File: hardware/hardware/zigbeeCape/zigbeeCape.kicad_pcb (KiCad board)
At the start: 4 copper layers, 63.5 x 54.6 mm, 160 parts, among them J1 Conn_ARM_JTAG_SWD_10, SW1 SW_MEC_5E, SW2 SW_MEC_5E, SW3 SW_MEC_5E, SW4 SW_MEC_5E, SW5 SW_MEC_5E, U1 CC1352R, U2 0.8Ghz_and_2.4GHz_Filter, U3 SMA_Antenna, U4 BeagleBone_P8, U5 BeagleBone_P9, Y1 32.768kHz, Y2 48MHz

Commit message: Almost done with traces
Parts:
- removed the REF** at (25.4, -8.89)
- removed the REF** at (33.1, -25.1)
- removed the REF** at (33.1, -27.7)
- removed the REF** at (33.1, -30.2)
- removed the REF** at (42.8, -14.1)
- removed the REF** at (42.2, -11.2)
- removed the REF** at (49.0, -14.6)
- removed the REF** at (27.1, -10.3)
- removed the REF** at (37.5, -7.49)
- removed the REF** at (28.6, -11.6)
- removed the REF** at (30.1, -13.1)
- removed the REF** at (31.8, -14.6)
- removed the REF** at (33.0, -15.9)
- removed the REF** at (33.1, -17.5)
- removed the REF** at (33.1, -20.1)
- removed the REF** at (33.1, -22.6)
- C10, C11, C13, C15, C16, C6, C8, C9, L1: moved to B.Cu
- moved C14 46.1 mm to (30.1, -21.6)
- moved C31 41.3 mm to (19.4, -30.0)
- moved Y1 39.9 mm to (31.5, -24.8), turned to 180 degrees
- moved C12 39.7 mm to (32.6, -21.6)
- moved R9 11.1 mm to (49.0, -37.6), turned to 90 degrees
- moved C13 9.39 mm to (38.5, -40.3), turned to 180 degrees
- moved R5 7.75 mm to (48.3, -30.7)
- moved C11 7.15 mm to (37.7, -43.6), turned to 180 degrees
- moved D3 6.98 mm to (48.4, -34.9)
- moved C5 6.55 mm to (43.1, -39.6), turned to 0 degrees
- moved C16 6.38 mm to (37.7, -41.9), turned to 180 degrees
- moved C8 4.66 mm to (41.9, -29.5), turned to 180 degrees
- moved Y2 3.68 mm to (39.9, -42.4), turned to 45 degrees
- moved C15 3.66 mm to (45.5, -29.5)
- moved C6 3.46 mm to (37.7, -29.5), turned to 180 degrees
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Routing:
- net SPI_CS: track 17.5 -> 38.0 mm
- net UART_RX: track 11.5 -> 29.0 mm
- net UART_TX: track 13.4 -> 30.2 mm
- net Net-(C14-Pad1): track 0.00 -> 16.4 mm
- net Net-(C12-Pad1): track 0.00 -> 15.2 mm
- net SPI_MISO: track 20.3 -> 33.2 mm
- net /ZigBeeFiltering/RX_TX: track 17.8 -> 8.64 mm, vias 3 -> 2
- net Cape_HeartBeat: track 10.8 -> 2.47 mm, vias 2 -> 0
- net Aux_1: track 14.9 -> 22.3 mm
- net VDDR: track 5.64 -> 11.8 mm, vias 0 -> 2
- net Aux_2: track 14.4 -> 20.1 mm
- net Net-(U1-Pad47): track 0.29 -> 5.15 mm
- net Net-(U1-Pad46): track 0.00 -> 4.84 mm
- net Net-(J1-Pad2): track 13.3 -> 17.8 mm
- net Net-(C15-Pad1): track 0.00 -> 4.32 mm, vias 0 -> 1
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
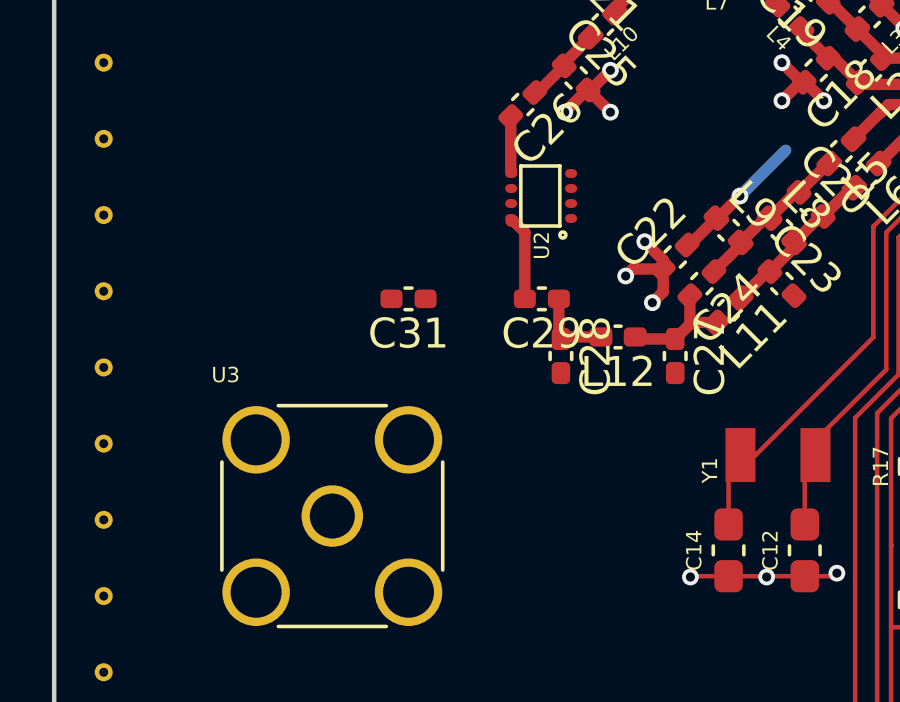
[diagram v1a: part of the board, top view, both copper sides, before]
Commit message: Finished traces, a couple problems with the design rules
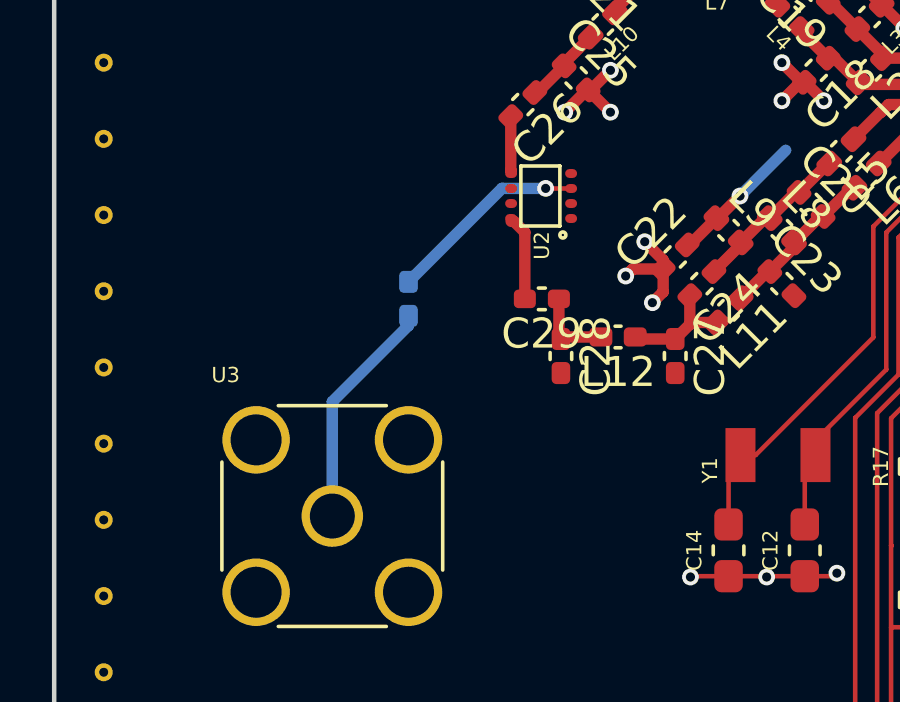
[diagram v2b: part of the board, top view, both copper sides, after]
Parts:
- C31: moved to B.Cu
- turned C31 to 270 degrees
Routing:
- net Net-(C31-Pad2): track 0.00 -> 7.79 mm
- net Net-(C31-Pad1): track 0.00 -> 6.71 mm, vias 0 -> 1

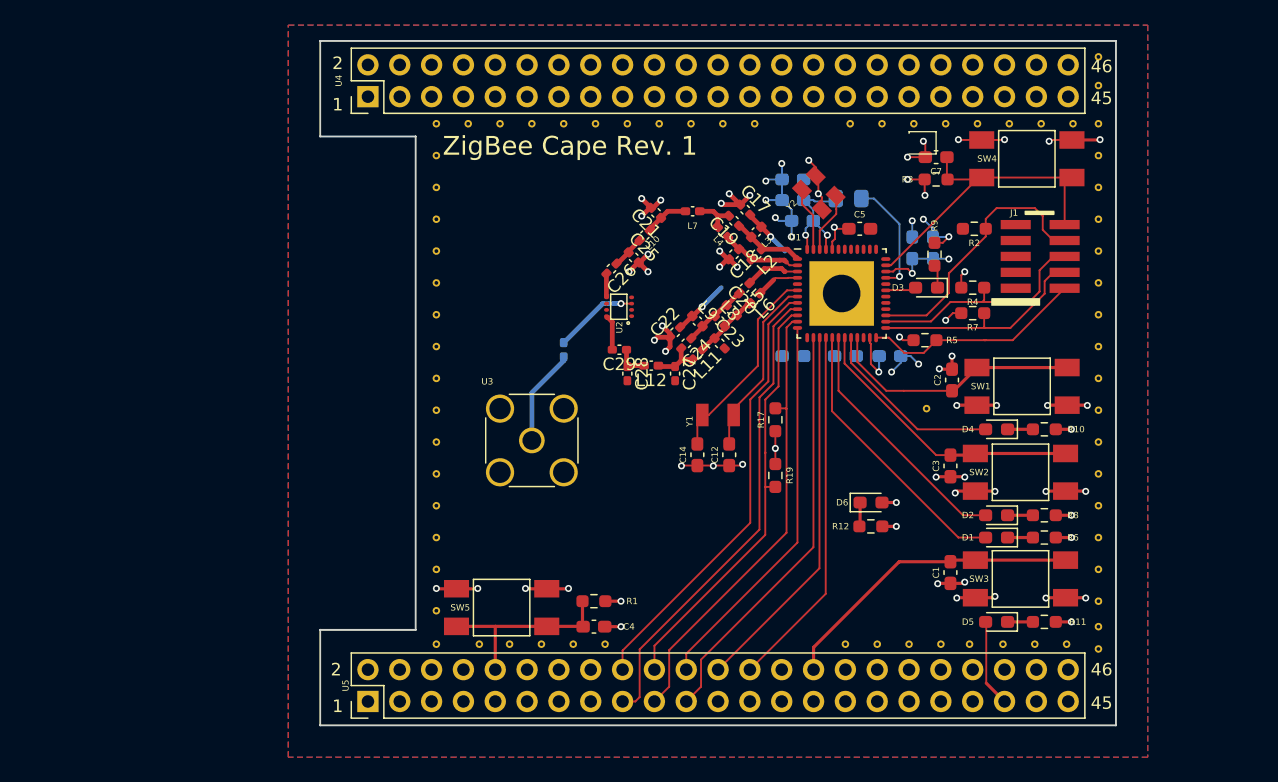
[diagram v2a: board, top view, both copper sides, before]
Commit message: Fixed some trace spacing things
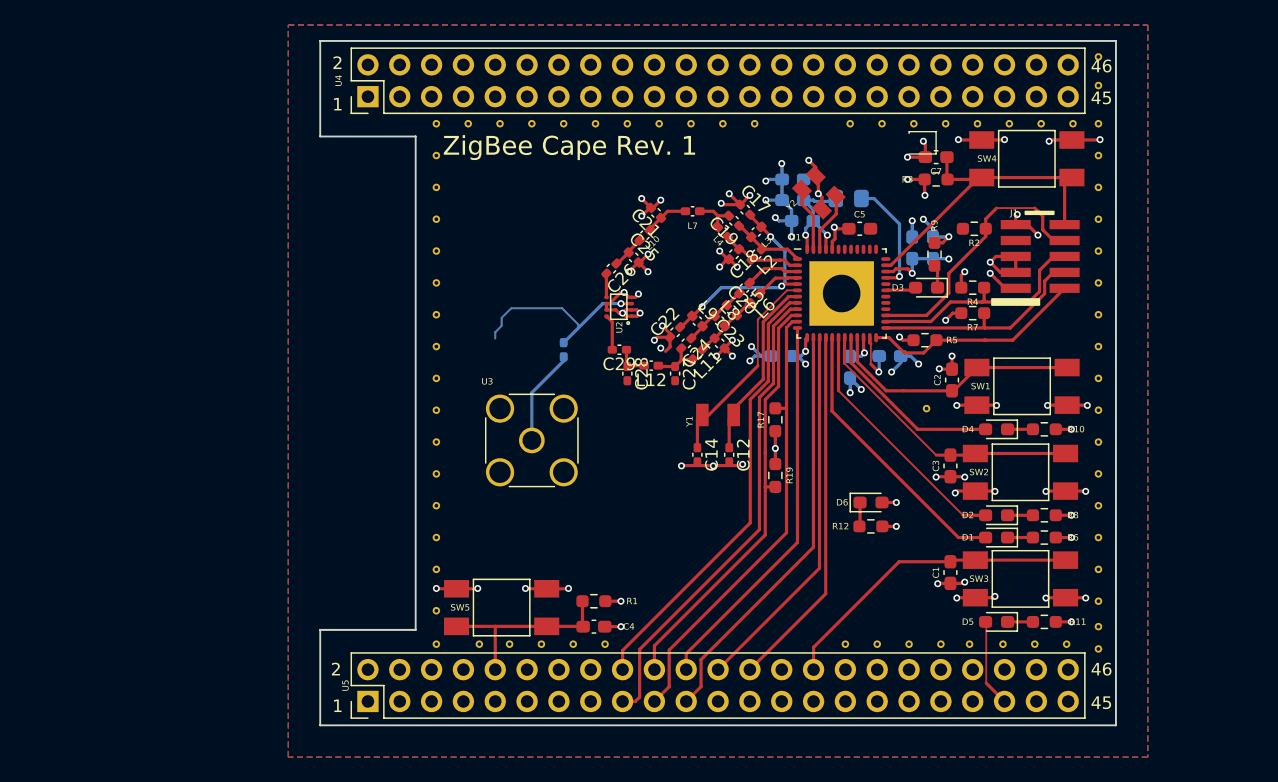
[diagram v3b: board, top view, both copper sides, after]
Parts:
- C12, C14: footprint Capacitor_SMD:C_0603_1608Metric_Pad1.08x0.95mm_HandSolder -> Capacitor_SMD:C_0402_1005Metric_Pad0.74x0.62mm_HandSolder
- R3: value DNM_10K -> DNM_10k
- moved C8 0.97 mm to (42.3, -28.6), turned to 270 degrees
- moved C6 0.89 mm to (36.8, -29.5)
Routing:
- net GND: track 99.9 -> 125.9 mm, vias 67 -> 81
- net Net-(C31-Pad1): track 6.71 -> 15.8 mm
- net /ZigBeeFiltering/RX_TX: track 8.64 -> 17.7 mm, vias 2 -> 3
- net +3V3: track 17.2 -> 25.9 mm, vias 8 -> 12
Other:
- net class Default: clearance 0.254 -> 0.1524
- net class HighSpeed added: clearance 0.127, trace_width 0.381, via_dia 0.5588, via_drill 0.3048
- rule trace_clearance: 0.254 -> 0.1524

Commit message: Finished up the stitching vias
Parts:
- added REF**: ViaStitch-0.6mm, zigbeeCape:ViaStitch-0.6mm, F.Cu at (46.9, -23.5)
- added REF**: ViaStitch-0.6mm, zigbeeCape:ViaStitch-0.6mm, F.Cu at (45.0, -43.2)
- added REF**: ViaStitch-0.6mm, zigbeeCape:ViaStitch-0.6mm, F.Cu at (9.27, -27.7)
- added REF**: ViaStitch-0.6mm, zigbeeCape:ViaStitch-0.6mm, F.Cu at (22.0, -30.2)
- added REF**: ViaStitch-0.6mm, zigbeeCape:ViaStitch-0.6mm, F.Cu at (16.9, -30.2)
- added REF**: ViaStitch-0.6mm, zigbeeCape:ViaStitch-0.6mm, F.Cu at (14.4, -30.2)
- added REF**: ViaStitch-0.6mm, zigbeeCape:ViaStitch-0.6mm, F.Cu at (11.8, -30.2)
- added REF**: ViaStitch-0.6mm, zigbeeCape:ViaStitch-0.6mm, F.Cu at (9.27, -30.2)
- added REF**: ViaStitch-0.6mm, zigbeeCape:ViaStitch-0.6mm, F.Cu at (19.4, -32.8)
- added REF**: ViaStitch-0.6mm, zigbeeCape:ViaStitch-0.6mm, F.Cu at (16.9, -32.8)
- added REF**: ViaStitch-0.6mm, zigbeeCape:ViaStitch-0.6mm, F.Cu at (14.4, -32.8)
- added REF**: ViaStitch-0.6mm, zigbeeCape:ViaStitch-0.6mm, F.Cu at (11.8, -32.8)
- added REF**: ViaStitch-0.6mm, zigbeeCape:ViaStitch-0.6mm, F.Cu at (42.3, -43.8)
- added REF**: ViaStitch-0.6mm, zigbeeCape:ViaStitch-0.6mm, F.Cu at (9.27, -32.8)
- added REF**: ViaStitch-0.6mm, zigbeeCape:ViaStitch-0.6mm, F.Cu at (21.6, -35.3)
- added REF**: ViaStitch-0.6mm, zigbeeCape:ViaStitch-0.6mm, F.Cu at (19.4, -35.3)
- added REF**: ViaStitch-0.6mm, zigbeeCape:ViaStitch-0.6mm, F.Cu at (16.9, -35.3)
- added REF**: ViaStitch-0.6mm, zigbeeCape:ViaStitch-0.6mm, F.Cu at (14.4, -35.3)
- added REF**: ViaStitch-0.6mm, zigbeeCape:ViaStitch-0.6mm, F.Cu at (11.8, -35.3)
- added REF**: ViaStitch-0.6mm, zigbeeCape:ViaStitch-0.6mm, F.Cu at (9.27, -35.3)
- added REF**: ViaStitch-0.6mm, zigbeeCape:ViaStitch-0.6mm, F.Cu at (22.0, -37.8)
- added REF**: ViaStitch-0.6mm, zigbeeCape:ViaStitch-0.6mm, F.Cu at (19.4, -37.8)
- added REF**: ViaStitch-0.6mm, zigbeeCape:ViaStitch-0.6mm, F.Cu at (16.9, -37.8)
- added REF**: ViaStitch-0.6mm, zigbeeCape:ViaStitch-0.6mm, F.Cu at (44.8, -45.5)
- added REF**: ViaStitch-0.6mm, zigbeeCape:ViaStitch-0.6mm, F.Cu at (14.4, -37.8)
- added REF**: ViaStitch-0.6mm, zigbeeCape:ViaStitch-0.6mm, F.Cu at (11.8, -37.8)
- added REF**: ViaStitch-0.6mm, zigbeeCape:ViaStitch-0.6mm, F.Cu at (9.27, -37.8)
- added REF**: ViaStitch-0.6mm, zigbeeCape:ViaStitch-0.6mm, F.Cu at (24.5, -40.4)
- added REF**: ViaStitch-0.6mm, zigbeeCape:ViaStitch-0.6mm, F.Cu at (22.0, -40.4)
- added REF**: ViaStitch-0.6mm, zigbeeCape:ViaStitch-0.6mm, F.Cu at (19.4, -40.4)
- added REF**: ViaStitch-0.6mm, zigbeeCape:ViaStitch-0.6mm, F.Cu at (16.9, -40.4)
- added REF**: ViaStitch-0.6mm, zigbeeCape:ViaStitch-0.6mm, F.Cu at (14.4, -40.4)
- added REF**: ViaStitch-0.6mm, zigbeeCape:ViaStitch-0.6mm, F.Cu at (11.8, -40.4)
- added REF**: ViaStitch-0.6mm, zigbeeCape:ViaStitch-0.6mm, F.Cu at (9.27, -40.4)
- added REF**: ViaStitch-0.6mm, zigbeeCape:ViaStitch-0.6mm, F.Cu at (42.3, -45.5)
- added REF**: ViaStitch-0.6mm, zigbeeCape:ViaStitch-0.6mm, F.Cu at (27.1, -42.9)
- added REF**: ViaStitch-0.6mm, zigbeeCape:ViaStitch-0.6mm, F.Cu at (24.5, -42.9)
- added REF**: ViaStitch-0.6mm, zigbeeCape:ViaStitch-0.6mm, F.Cu at (22.0, -42.9)
- added REF**: ViaStitch-0.6mm, zigbeeCape:ViaStitch-0.6mm, F.Cu at (19.4, -42.9)
- added REF**: ViaStitch-0.6mm, zigbeeCape:ViaStitch-0.6mm, F.Cu at (16.9, -42.9)
- added REF**: ViaStitch-0.6mm, zigbeeCape:ViaStitch-0.6mm, F.Cu at (14.4, -42.9)
- added REF**: ViaStitch-0.6mm, zigbeeCape:ViaStitch-0.6mm, F.Cu at (11.8, -42.9)
- added REF**: ViaStitch-0.6mm, zigbeeCape:ViaStitch-0.6mm, F.Cu at (9.27, -42.9)
- added REF**: ViaStitch-0.6mm, zigbeeCape:ViaStitch-0.6mm, F.Cu at (27.1, -45.5)
- added REF**: ViaStitch-0.6mm, zigbeeCape:ViaStitch-0.6mm, F.Cu at (24.5, -45.5)
- added REF**: ViaStitch-0.6mm, zigbeeCape:ViaStitch-0.6mm, F.Cu at (44.8, -48.0)
- added REF**: ViaStitch-0.6mm, zigbeeCape:ViaStitch-0.6mm, F.Cu at (22.0, -45.5)
- added REF**: ViaStitch-0.6mm, zigbeeCape:ViaStitch-0.6mm, F.Cu at (19.4, -45.5)
- added REF**: ViaStitch-0.6mm, zigbeeCape:ViaStitch-0.6mm, F.Cu at (16.9, -45.5)
- added REF**: ViaStitch-0.6mm, zigbeeCape:ViaStitch-0.6mm, F.Cu at (14.4, -45.5)
- added REF**: ViaStitch-0.6mm, zigbeeCape:ViaStitch-0.6mm, F.Cu at (11.8, -45.5)
- added REF**: ViaStitch-0.6mm, zigbeeCape:ViaStitch-0.6mm, F.Cu at (9.27, -45.5)
- added REF**: ViaStitch-0.6mm, zigbeeCape:ViaStitch-0.6mm, F.Cu at (27.1, -48.0)
- added REF**: ViaStitch-0.6mm, zigbeeCape:ViaStitch-0.6mm, F.Cu at (24.5, -48.0)
- added REF**: ViaStitch-0.6mm, zigbeeCape:ViaStitch-0.6mm, F.Cu at (22.0, -48.0)
- added REF**: ViaStitch-0.6mm, zigbeeCape:ViaStitch-0.6mm, F.Cu at (19.4, -48.0)
- added REF**: ViaStitch-0.6mm, zigbeeCape:ViaStitch-0.6mm, F.Cu at (34.3, -43.6)
- added REF**: ViaStitch-0.6mm, zigbeeCape:ViaStitch-0.6mm, F.Cu at (16.9, -48.0)
- added REF**: ViaStitch-0.6mm, zigbeeCape:ViaStitch-0.6mm, F.Cu at (14.4, -48.0)
- added REF**: ViaStitch-0.6mm, zigbeeCape:ViaStitch-0.6mm, F.Cu at (11.8, -48.0)
- added REF**: ViaStitch-0.6mm, zigbeeCape:ViaStitch-0.6mm, F.Cu at (52.3, -42.8)
- added REF**: ViaStitch-0.6mm, zigbeeCape:ViaStitch-0.6mm, F.Cu at (56.4, -43.7)
- added REF**: ViaStitch-0.6mm, zigbeeCape:ViaStitch-0.6mm, F.Cu at (58.3, -42.4)
- added REF**: ViaStitch-0.6mm, zigbeeCape:ViaStitch-0.6mm, F.Cu at (51.6, -46.4)
- added REF**: ViaStitch-0.6mm, zigbeeCape:ViaStitch-0.6mm, F.Cu at (54.7, -46.0)
- added REF**: ViaStitch-0.6mm, zigbeeCape:ViaStitch-0.6mm, F.Cu at (57.9, -45.8)
- added REF**: ViaStitch-0.6mm, zigbeeCape:ViaStitch-0.6mm, F.Cu at (60.1, -31.4)
- added REF**: ViaStitch-0.6mm, zigbeeCape:ViaStitch-0.6mm, F.Cu at (31.8, -43.6)
- added REF**: ViaStitch-0.6mm, zigbeeCape:ViaStitch-0.6mm, F.Cu at (59.8, -34.4)
- added REF**: ViaStitch-0.6mm, zigbeeCape:ViaStitch-0.6mm, F.Cu at (57.7, -32.6)
- added REF**: ViaStitch-0.6mm, zigbeeCape:ViaStitch-0.6mm, F.Cu at (57.7, -30.7)
- added REF**: ViaStitch-0.6mm, zigbeeCape:ViaStitch-0.6mm, F.Cu at (54.5, -30.6)
- added REF**: ViaStitch-0.6mm, zigbeeCape:ViaStitch-0.6mm, F.Cu at (57.4, -28.3)
- added REF**: ViaStitch-0.6mm, zigbeeCape:ViaStitch-0.6mm, F.Cu at (54.4, -28.4)
- added REF**: ViaStitch-0.6mm, zigbeeCape:ViaStitch-0.6mm, F.Cu at (57.4, -21.5)
- added REF**: ViaStitch-0.6mm, zigbeeCape:ViaStitch-0.6mm, F.Cu at (54.2, -21.5)
- added REF**: ViaStitch-0.6mm, zigbeeCape:ViaStitch-0.6mm, F.Cu at (44.6, -9.91)
- added REF**: ViaStitch-0.6mm, zigbeeCape:ViaStitch-0.6mm, F.Cu at (47.2, -12.2)
- added REF**: ViaStitch-0.6mm, zigbeeCape:ViaStitch-0.6mm, F.Cu at (29.6, -42.9)
- added REF**: ViaStitch-0.6mm, zigbeeCape:ViaStitch-0.6mm, F.Cu at (50.3, -9.40)
- added REF**: ViaStitch-0.6mm, zigbeeCape:ViaStitch-0.6mm, F.Cu at (46.5, -15.5)
- added REF**: ViaStitch-0.6mm, zigbeeCape:ViaStitch-0.6mm, F.Cu at (49.1, -15.7)
- added REF**: ViaStitch-0.6mm, zigbeeCape:ViaStitch-0.6mm, F.Cu at (42.7, -14.4)
- added REF**: ViaStitch-0.6mm, zigbeeCape:ViaStitch-0.6mm, F.Cu at (42.5, -21.0)
- added REF**: ViaStitch-0.6mm, zigbeeCape:ViaStitch-0.6mm, F.Cu at (41.5, -23.5)
- added REF**: ViaStitch-0.6mm, zigbeeCape:ViaStitch-0.6mm, F.Cu at (41.3, -10.7)
- added REF**: ViaStitch-0.6mm, zigbeeCape:ViaStitch-0.6mm, F.Cu at (38.1, -7.37)
- added REF**: ViaStitch-0.6mm, zigbeeCape:ViaStitch-0.6mm, F.Cu at (57.5, -12.1)
- added REF**: ViaStitch-0.6mm, zigbeeCape:ViaStitch-0.6mm, F.Cu at (54.2, -12.1)
- added REF**: ViaStitch-0.6mm, zigbeeCape:ViaStitch-0.6mm, F.Cu at (34.7, -45.5)
- added REF**: ViaStitch-0.6mm, zigbeeCape:ViaStitch-0.6mm, F.Cu at (32.1, -45.5)
- added REF**: ViaStitch-0.6mm, zigbeeCape:ViaStitch-0.6mm, F.Cu at (44.2, -26.2)
- added REF**: ViaStitch-0.6mm, zigbeeCape:ViaStitch-0.6mm, F.Cu at (29.6, -45.5)
- added REF**: ViaStitch-0.6mm, zigbeeCape:ViaStitch-0.6mm, F.Cu at (34.7, -48.0)
- added REF**: ViaStitch-0.6mm, zigbeeCape:ViaStitch-0.6mm, F.Cu at (32.1, -48.0)
- added REF**: ViaStitch-0.6mm, zigbeeCape:ViaStitch-0.6mm, F.Cu at (25.3, -36.4)
- added REF**: ViaStitch-0.6mm, zigbeeCape:ViaStitch-0.6mm, F.Cu at (28.2, -36.6)
- added REF**: ViaStitch-0.6mm, zigbeeCape:ViaStitch-0.6mm, F.Cu at (26.7, -35.3)
- added REF**: ViaStitch-0.6mm, zigbeeCape:ViaStitch-0.6mm, F.Cu at (27.6, -38.0)
- added REF**: ViaStitch-0.6mm, zigbeeCape:ViaStitch-0.6mm, F.Cu at (30.5, -37.6)
- added REF**: ViaStitch-0.6mm, zigbeeCape:ViaStitch-0.6mm, F.Cu at (29.2, -39.1)
- added REF**: ViaStitch-0.6mm, zigbeeCape:ViaStitch-0.6mm, F.Cu at (27.3, -39.6)
- added REF**: ViaStitch-0.6mm, zigbeeCape:ViaStitch-0.6mm, F.Cu at (47.1, -28.6)
- added REF**: ViaStitch-0.6mm, zigbeeCape:ViaStitch-0.6mm, F.Cu at (28.4, -40.8)
- added REF**: ViaStitch-0.6mm, zigbeeCape:ViaStitch-0.6mm, F.Cu at (30.1, -40.8)
- added REF**: ViaStitch-0.6mm, zigbeeCape:ViaStitch-0.6mm, F.Cu at (31.1, -39.5)
- added REF**: ViaStitch-0.6mm, zigbeeCape:ViaStitch-0.6mm, F.Cu at (32.8, -36.7)
- added REF**: ViaStitch-0.6mm, zigbeeCape:ViaStitch-0.6mm, F.Cu at (29.7, -35.7)
- added REF**: ViaStitch-0.6mm, zigbeeCape:ViaStitch-0.6mm, F.Cu at (27.9, -34.3)
- added REF**: ViaStitch-0.6mm, zigbeeCape:ViaStitch-0.6mm, F.Cu at (26.0, -32.9)
- added REF**: ViaStitch-0.6mm, zigbeeCape:ViaStitch-0.6mm, F.Cu at (25.8, -31.0)
- added REF**: ViaStitch-0.6mm, zigbeeCape:ViaStitch-0.6mm, F.Cu at (24.4, -32.3)
- added REF**: ViaStitch-0.6mm, zigbeeCape:ViaStitch-0.6mm, F.Cu at (30.2, -29.0)
- added REF**: ViaStitch-0.6mm, zigbeeCape:ViaStitch-0.6mm, F.Cu at (47.2, -34.5)
- added REF**: ViaStitch-0.6mm, zigbeeCape:ViaStitch-0.6mm, F.Cu at (32.6, -29.2)
- added REF**: ViaStitch-0.6mm, zigbeeCape:ViaStitch-0.6mm, F.Cu at (31.2, -27.8)
- added REF**: ViaStitch-0.6mm, zigbeeCape:ViaStitch-0.6mm, F.Cu at (28.7, -27.4)
- added REF**: ViaStitch-0.6mm, zigbeeCape:ViaStitch-0.6mm, F.Cu at (28.8, -24.9)
- added REF**: ViaStitch-0.6mm, zigbeeCape:ViaStitch-0.6mm, F.Cu at (25.7, -11.3)
- added REF**: ViaStitch-0.6mm, zigbeeCape:ViaStitch-0.6mm, F.Cu at (15.9, -10.2)
- added REF**: ViaStitch-0.6mm, zigbeeCape:ViaStitch-0.6mm, F.Cu at (13.0, -10.2)
- added REF**: ViaStitch-0.6mm, zigbeeCape:ViaStitch-0.6mm, F.Cu at (31.8, -17.4)
- added REF**: ViaStitch-0.6mm, zigbeeCape:ViaStitch-0.6mm, F.Cu at (31.8, -19.8)
- added REF**: ViaStitch-0.6mm, zigbeeCape:ViaStitch-0.6mm, F.Cu at (29.6, -21.0)
- added REF**: ViaStitch-0.6mm, zigbeeCape:ViaStitch-0.6mm, F.Cu at (40.1, -46.7)
- added REF**: ViaStitch-0.6mm, zigbeeCape:ViaStitch-0.6mm, F.Cu at (29.5, -18.5)
- added REF**: ViaStitch-0.6mm, zigbeeCape:ViaStitch-0.6mm, F.Cu at (29.5, -16.0)
- added REF**: ViaStitch-0.6mm, zigbeeCape:ViaStitch-0.6mm, F.Cu at (27.1, -12.4)
- added REF**: ViaStitch-0.6mm, zigbeeCape:ViaStitch-0.6mm, F.Cu at (24.5, -12.4)
- added REF**: ViaStitch-0.6mm, zigbeeCape:ViaStitch-0.6mm, F.Cu at (22.0, -12.4)
- added REF**: ViaStitch-0.6mm, zigbeeCape:ViaStitch-0.6mm, F.Cu at (19.4, -12.4)
- added REF**: ViaStitch-0.6mm, zigbeeCape:ViaStitch-0.6mm, F.Cu at (16.9, -12.4)
- added REF**: ViaStitch-0.6mm, zigbeeCape:ViaStitch-0.6mm, F.Cu at (14.4, -12.4)
- added REF**: ViaStitch-0.6mm, zigbeeCape:ViaStitch-0.6mm, F.Cu at (11.8, -12.4)
- added REF**: ViaStitch-0.6mm, zigbeeCape:ViaStitch-0.6mm, F.Cu at (9.27, -12.4)
- added REF**: ViaStitch-0.6mm, zigbeeCape:ViaStitch-0.6mm, F.Cu at (37.6, -47.0)
- added REF**: ViaStitch-0.6mm, zigbeeCape:ViaStitch-0.6mm, F.Cu at (27.1, -15.0)
- added REF**: ViaStitch-0.6mm, zigbeeCape:ViaStitch-0.6mm, F.Cu at (24.5, -15.0)
- added REF**: ViaStitch-0.6mm, zigbeeCape:ViaStitch-0.6mm, F.Cu at (22.0, -15.0)
- added REF**: ViaStitch-0.6mm, zigbeeCape:ViaStitch-0.6mm, F.Cu at (19.4, -15.0)
- added REF**: ViaStitch-0.6mm, zigbeeCape:ViaStitch-0.6mm, F.Cu at (16.9, -15.0)
- added REF**: ViaStitch-0.6mm, zigbeeCape:ViaStitch-0.6mm, F.Cu at (14.4, -15.0)
- added REF**: ViaStitch-0.6mm, zigbeeCape:ViaStitch-0.6mm, F.Cu at (11.8, -15.0)
- added REF**: ViaStitch-0.6mm, zigbeeCape:ViaStitch-0.6mm, F.Cu at (9.27, -15.0)
- added REF**: ViaStitch-0.6mm, zigbeeCape:ViaStitch-0.6mm, F.Cu at (27.1, -17.5)
- added REF**: ViaStitch-0.6mm, zigbeeCape:ViaStitch-0.6mm, F.Cu at (24.5, -17.5)
- added REF**: ViaStitch-0.6mm, zigbeeCape:ViaStitch-0.6mm, F.Cu at (40.1, -49.0)
- added REF**: ViaStitch-0.6mm, zigbeeCape:ViaStitch-0.6mm, F.Cu at (22.0, -17.5)
- added REF**: ViaStitch-0.6mm, zigbeeCape:ViaStitch-0.6mm, F.Cu at (19.4, -17.5)
- added REF**: ViaStitch-0.6mm, zigbeeCape:ViaStitch-0.6mm, F.Cu at (16.9, -17.5)
- added REF**: ViaStitch-0.6mm, zigbeeCape:ViaStitch-0.6mm, F.Cu at (14.4, -17.5)
- added REF**: ViaStitch-0.6mm, zigbeeCape:ViaStitch-0.6mm, F.Cu at (11.8, -17.5)
- added REF**: ViaStitch-0.6mm, zigbeeCape:ViaStitch-0.6mm, F.Cu at (9.27, -17.5)
- added REF**: ViaStitch-0.6mm, zigbeeCape:ViaStitch-0.6mm, F.Cu at (27.1, -20.1)
- added REF**: ViaStitch-0.6mm, zigbeeCape:ViaStitch-0.6mm, F.Cu at (24.5, -20.1)
- added REF**: ViaStitch-0.6mm, zigbeeCape:ViaStitch-0.6mm, F.Cu at (22.0, -20.1)
- added REF**: ViaStitch-0.6mm, zigbeeCape:ViaStitch-0.6mm, F.Cu at (16.9, -20.1)
- added REF**: ViaStitch-0.6mm, zigbeeCape:ViaStitch-0.6mm, F.Cu at (37.6, -49.0)
- added REF**: ViaStitch-0.6mm, zigbeeCape:ViaStitch-0.6mm, F.Cu at (11.8, -20.1)
- added REF**: ViaStitch-0.6mm, zigbeeCape:ViaStitch-0.6mm, F.Cu at (9.27, -20.1)
- added REF**: ViaStitch-0.6mm, zigbeeCape:ViaStitch-0.6mm, F.Cu at (27.1, -22.6)
- added REF**: ViaStitch-0.6mm, zigbeeCape:ViaStitch-0.6mm, F.Cu at (24.5, -22.6)
- added REF**: ViaStitch-0.6mm, zigbeeCape:ViaStitch-0.6mm, F.Cu at (22.0, -22.6)
- added REF**: ViaStitch-0.6mm, zigbeeCape:ViaStitch-0.6mm, F.Cu at (19.4, -22.6)
- added REF**: ViaStitch-0.6mm, zigbeeCape:ViaStitch-0.6mm, F.Cu at (14.4, -22.6)
- added REF**: ViaStitch-0.6mm, zigbeeCape:ViaStitch-0.6mm, F.Cu at (11.8, -22.6)
- added REF**: ViaStitch-0.6mm, zigbeeCape:ViaStitch-0.6mm, F.Cu at (9.27, -22.6)
- added REF**: ViaStitch-0.6mm, zigbeeCape:ViaStitch-0.6mm, F.Cu at (27.1, -25.1)
- added REF**: ViaStitch-0.6mm, zigbeeCape:ViaStitch-0.6mm, F.Cu at (46.6, -42.7)
- added REF**: ViaStitch-0.6mm, zigbeeCape:ViaStitch-0.6mm, F.Cu at (24.5, -25.1)
- added REF**: ViaStitch-0.6mm, zigbeeCape:ViaStitch-0.6mm, F.Cu at (22.0, -25.1)
- added REF**: ViaStitch-0.6mm, zigbeeCape:ViaStitch-0.6mm, F.Cu at (11.8, -25.1)
- added REF**: ViaStitch-0.6mm, zigbeeCape:ViaStitch-0.6mm, F.Cu at (9.27, -25.1)
- added REF**: ViaStitch-0.6mm, zigbeeCape:ViaStitch-0.6mm, F.Cu at (27.1, -27.7)
- added REF**: ViaStitch-0.6mm, zigbeeCape:ViaStitch-0.6mm, F.Cu at (22.0, -27.7)
- added REF**: ViaStitch-0.6mm, zigbeeCape:ViaStitch-0.6mm, F.Cu at (19.4, -27.7)
- added REF**: ViaStitch-0.6mm, zigbeeCape:ViaStitch-0.6mm, F.Cu at (16.9, -27.7)
- added REF**: ViaStitch-0.6mm, zigbeeCape:ViaStitch-0.6mm, F.Cu at (14.4, -27.7)
- added REF**: ViaStitch-0.6mm, zigbeeCape:ViaStitch-0.6mm, F.Cu at (11.8, -27.7)
- moved U3 0.13 mm to (16.9, -22.6)
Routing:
- net Net-(C31-Pad1): track 15.8 -> 6.97 mm

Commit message: Fix silk screen, fixed via stitching net
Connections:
- REF** pad 1: (no net) -> GND (x65)

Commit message: Added gerber files
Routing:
- added copper zone on +3.3V, net GND

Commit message: Fixed micro, filter, push button footprints and fixed layout
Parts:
- moved Y2 0.28 mm to (40.2, -42.4)
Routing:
- net GND: track 125.9 -> 120.7 mm, vias 81 -> 80
- net Net-(U1-Pad47): track 5.15 -> 4.35 mm
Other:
- rule trace_min: 0.1524 -> 0.254
